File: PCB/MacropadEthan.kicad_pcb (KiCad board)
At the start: 2 copper layers, 95 x 95 mm, 36 parts, among them SW1 SW_Push, SW10 SW_Push, SW11 SW_Push, SW12 SW_Push, SW2 RotaryEncoder_Switch, SW3 SW_Push, SW4 SW_Push, SW5 SW_Push, SW6 SW_Push, SW7 SW_Push, SW8 SW_Push, SW9 SW_Push, U1 MOUDLE-SEEEDUINO-XIAO

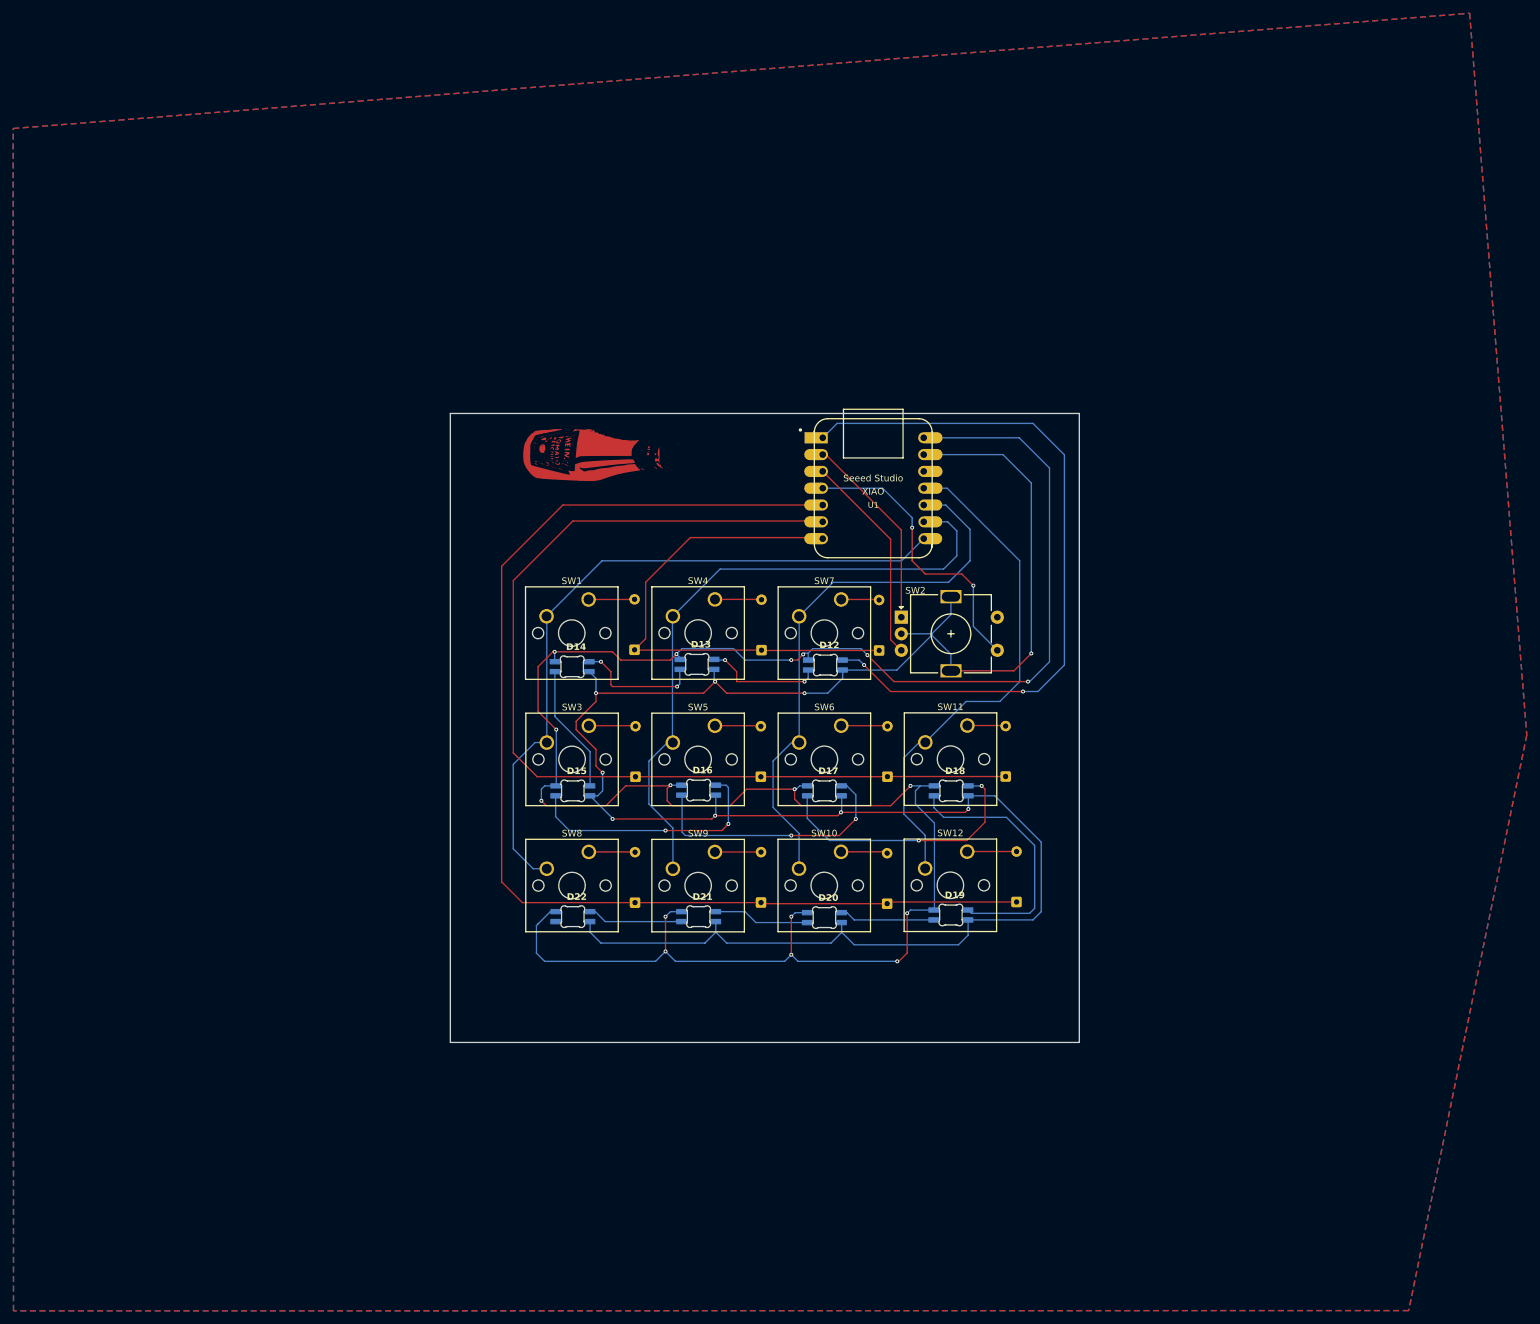
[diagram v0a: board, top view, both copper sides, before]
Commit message: changed files
changed PCB silkscreen and updated warnings / errors when checking design rules checker
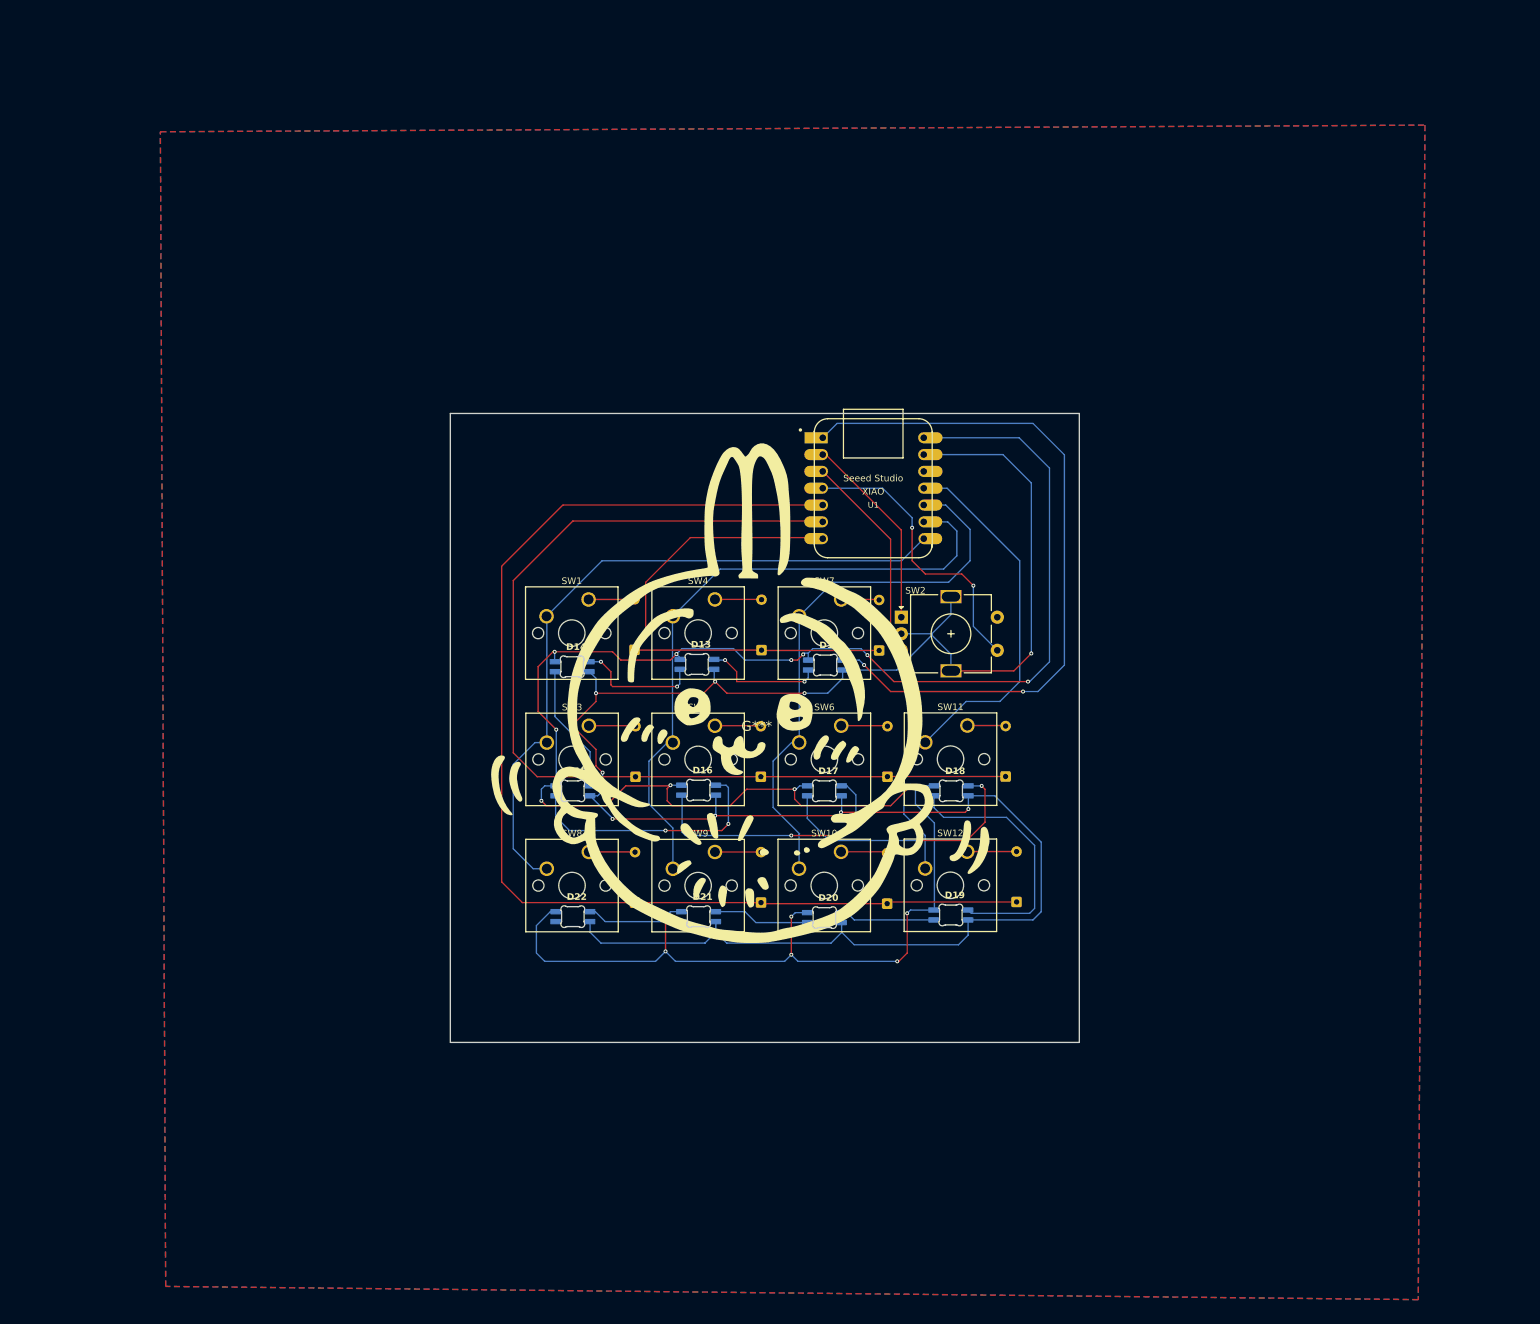
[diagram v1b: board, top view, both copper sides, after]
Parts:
- moved G*** 48.7 mm to (99.3, 65.0)
